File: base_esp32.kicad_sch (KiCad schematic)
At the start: 67 parts, among them J1 Input Source, J10 5V, J11 keypad, J12 keypad, J13 H_IO33, J14 H_IO15, J15 H_IO32, J16 H_IO02, J17 H_IO04, J18 H_IO33_OUT, J19 H_IO15_OUT, J2 Src Board, J20 H_IO32_OUT, J21 H_IO02_OUT, J22 H_IO04_OUT, J23 I2C, J24 I2C, J25 SPI, J26 SPI, J27 IO34, J28 IO35, J29 IO36, J3 5V, J30 IO39, J31 bypass, J4 5V, J5 5V, J6 5V, J7 5V, J8 5V, J9 5V, SW1 SW_DIP_KEYPAD, SW2 SW_DIP_INPUTS, SW3 Selector_Input, SW4 Selector_Input, SW5 INPUT_1, SW6 INPUT_2, SW7 RESET, SW8 BOOT, U1 LM7805_TO220, U2 ESP32-DevKitC, U3 AMS1117, U4 AMS1117

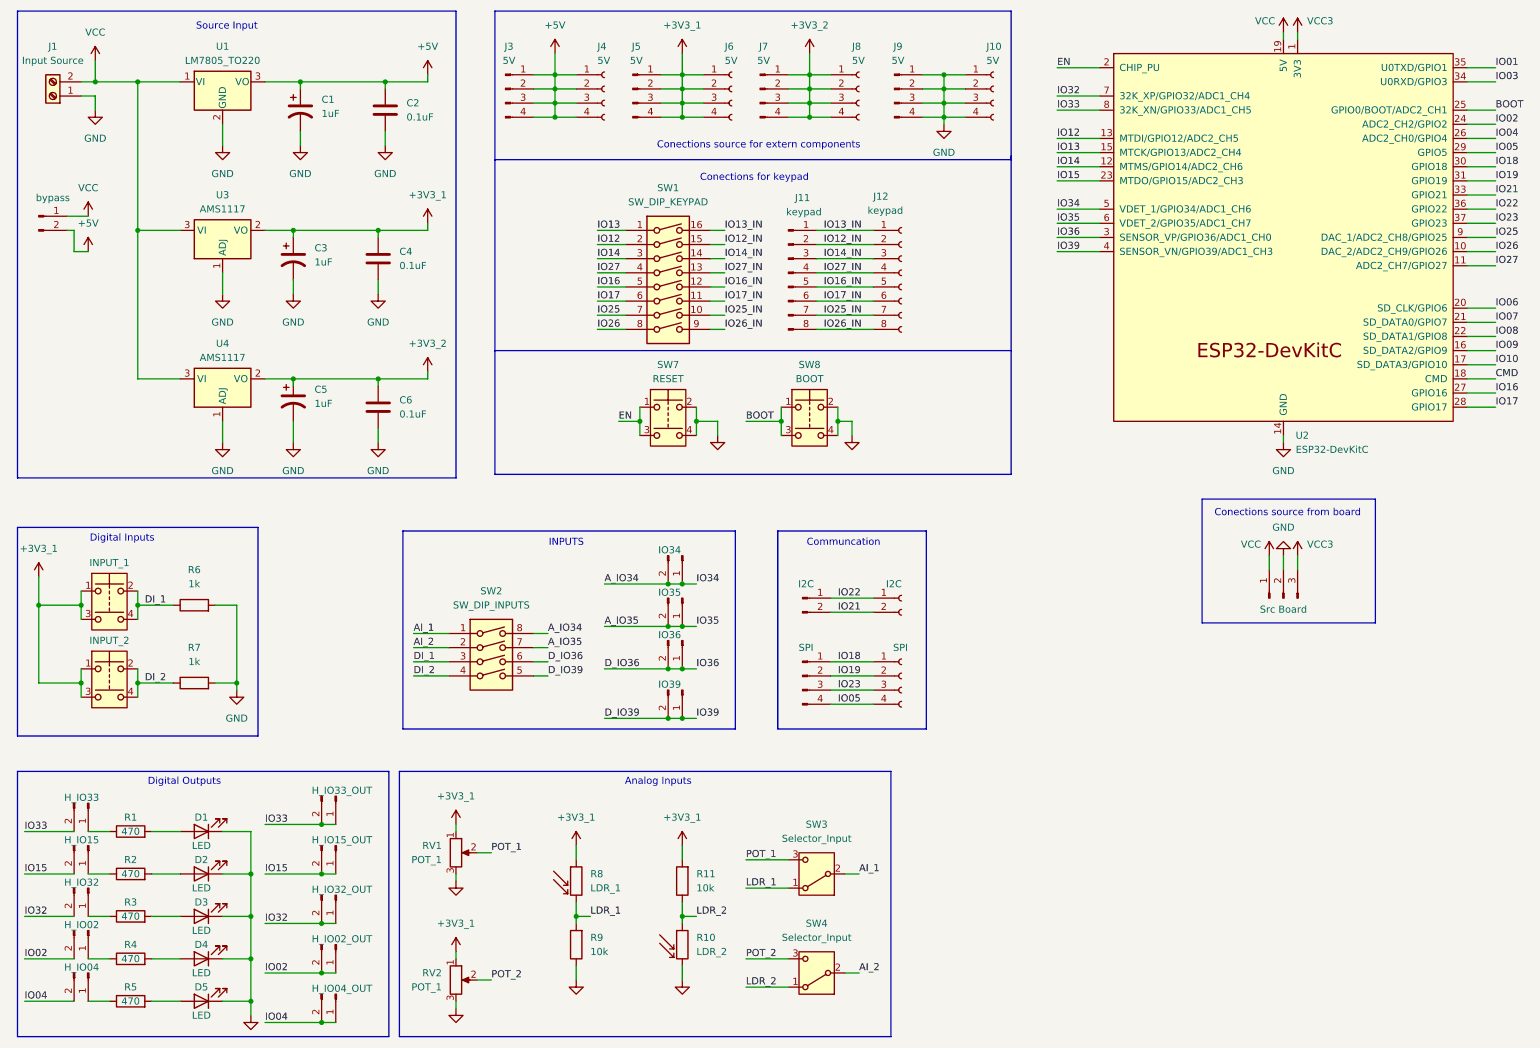
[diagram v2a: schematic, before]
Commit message: fix: vpp for board
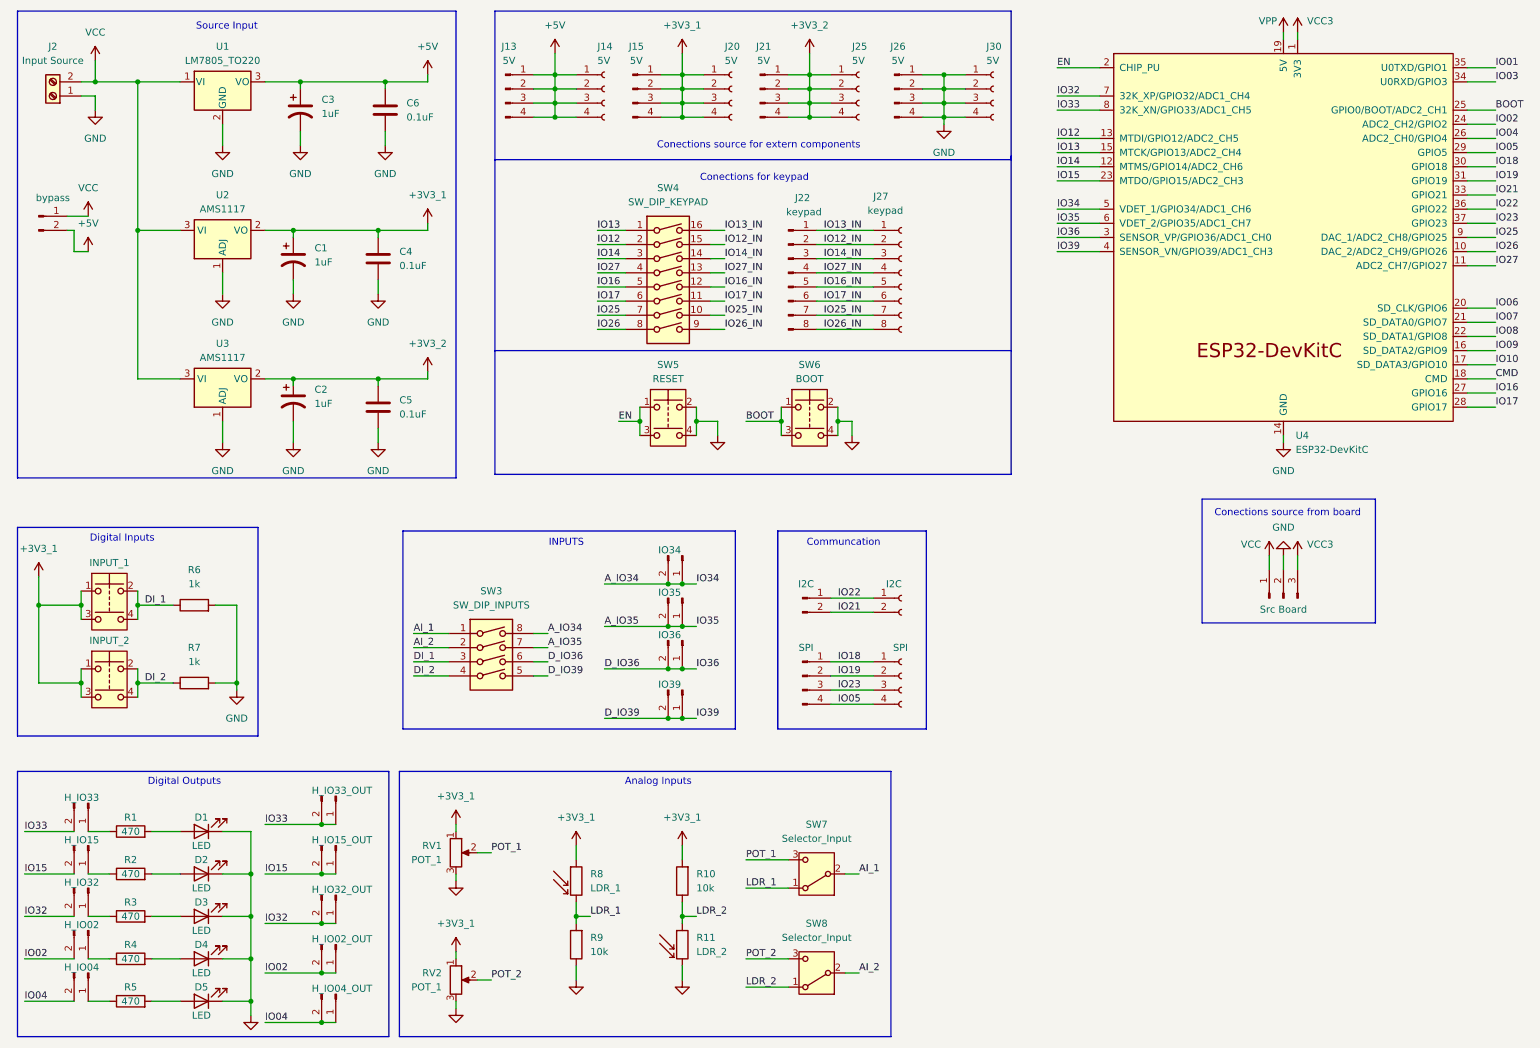
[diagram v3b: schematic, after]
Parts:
- renumbered C3 to C1, C5 to C2, C1 to C3, C6 to C5, C2 to C6, J31 to J1, J20 to J10, J21 to J11, J22 to J12, J3 to J13, J4 to J14, J5 to J15, J27 to J16, J28 to J17, J29 to J18, J30 to J19, J1 to J2, J6 to J20, J7 to J21, J11 to J22, J25 to J24, J8 to J25, J9 to J26, J12 to J27, J24 to J28, J26 to J29, J13 to J3, J10 to J30, J2 to J31, J14 to J4, J15 to J5, J16 to J6, J17 to J7, J18 to J8, J19 to J9, R11 to R10, R10 to R11, SW5 to SW1, SW6 to SW2, SW2 to SW3, SW1 to SW4, SW7 to SW5, SW8 to SW6, SW3 to SW7, SW4 to SW8, U3 to U2, U4 to U3, U2 to U4
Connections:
- net VCC: no longer U4.19 (5V)
- new net VPP: U4.19 (5V)

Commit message: fix: ERC
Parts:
- added J32: TX_RX, symbol Connector:Conn_01x02_Pin
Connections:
- net A_IO34 renamed IO34
- net A_IO35 renamed IO35
- net CMD: no longer names the net of U4.18 (CMD)
- net D_IO36 renamed IO36
- net D_IO39 renamed IO39
- net IO01 renamed TX
- net TX: now also J32.1 (Pin_1)
- net IO03 renamed RX
- net RX: now also J32.2 (Pin_2)
- net IO06: no longer names the net of U4.20 (SD_CLK/GPIO6)
- net IO07: no longer names the net of U4.21 (SD_DATA0/GPIO7)
- net IO08: no longer names the net of U4.22 (SD_DATA1/GPIO8)
- net IO09: no longer names the net of U4.16 (SD_DATA2/GPIO9)
- net IO10: no longer names the net of U4.17 (SD_DATA3/GPIO10)
- no-connect marks 0 -> 6
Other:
- note added: "Communication"
- note removed: "Communcation"

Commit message: add: footprints, not done yet
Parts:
- D1, D2, D3, D4, D5: footprint (none) -> LED_THT:LED_D3.0mm
- J1, J10, J11, J12, J16, J17, J18, J19, J23, J3, J32, J4, J5, J6, J7, J8, J9: footprint (none) -> Connector_PinHeader_1.27mm:PinHeader_1x02_P1.27mm_Vertical
- J13, J15, J21, J24, J26: footprint (none) -> Connector_PinHeader_1.27mm:PinHeader_1x04_P1.27mm_Vertical
- J14, J20, J25, J29, J30: footprint (none) -> Connector_PinSocket_1.27mm:PinSocket_1x04_P1.27mm_Vertical
- J2: footprint (none) -> TerminalBlock:TerminalBlock_Xinya_XY308-2.54-2P_1x02_P2.54mm_Horizontal
- J22: footprint (none) -> Connector_PinHeader_1.27mm:PinHeader_1x08_P1.27mm_Vertical
- J27: footprint (none) -> Connector_PinSocket_1.27mm:PinSocket_1x08_P1.27mm_Vertical
- J28: footprint (none) -> Connector_PinSocket_1.27mm:PinSocket_1x02_P1.27mm_Vertical
- J31: footprint (none) -> Connector_PinHeader_1.27mm:PinHeader_1x03_P1.27mm_Vertical
- RV1, RV2: footprint (none) -> Potentiometer_THT:Potentiometer_Alps_RK163_Single_Horizontal
- SW1, SW2, SW5, SW6: footprint (none) -> Button_Switch_THT:SW_PUSH_6mm
- SW3, SW4: footprint (none) -> Button_Switch_THT:SW_DIP_SPSTx04_Slide_9.78x12.34mm_W7.62mm_P2.54mm
- SW7, SW8: footprint (none) -> Button_Switch_THT:SW_Slide-03_Wuerth-WS-SLTV_10x2.5x6.4_P2.54mm
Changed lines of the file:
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@@
 			)
 		)
-		(property "Footprint" ""
+		(property "Footprint" "Connector_PinHeader_1.27mm:PinHeader_1x02_P1.27mm_Vertical"
 			(at 158.75 137.16 0)
 			(effects
@@
 			)
 		)
-		(property "Footprint" ""
+		(property "Footprint" "Connector_PinHeader_1.27mm:PinHeader_1x04_P1.27mm_Vertical"
 			(at 146.05 26.67 0)
 			(effects
@@
 			)
 		)
-		(property "Footprint" ""
+		(property "Footprint" "Connector_PinSocket_1.27mm:PinSocket_1x04_P1.27mm_Vertical"
 			(at 163.83 26.67 0)
 			(effects
@@
 			)
 		)
-		(property "Footprint" ""
+		(property "Footprint" "Connector_PinHeader_1.27mm:PinHeader_1x03_P1.27mm_Vertical"
 			(at 240.03 118.11 0)
 			(effects
@@
 			)
 		)
-		(property "Footprint" ""
+		(property "Footprint" "Connector_PinHeader_1.27mm:PinHeader_1x02_P1.27mm_Vertical"
 			(at 25.4 162.56 0)
 			(effects
@@
 			)
 		)
-		(property "Footprint" ""
+		(property "Footprint" "LED_THT:LED_D3.0mm"
 			(at 45.72 175.26 0)
 			(effects
@@
 			)
 		)
-		(property "Footprint" ""
+		(property "Footprint" "Connector_PinHeader_1.27mm:PinHeader_1x04_P1.27mm_Vertical"
 			(at 153.67 125.73 0)
 			(effects
@@
 			)
 		)
-		(property "Footprint" ""
+		(property "Footprint" "Connector_PinHeader_1.27mm:PinHeader_1x04_P1.27mm_Vertical"
 			(at 170.18 26.67 0)
 			(effects
@@
 			)
 		)
-		(property "Footprint" ""
+		(property "Footprint" "Button_Switch_THT:SW_DIP_SPSTx04_Slide_9.78x12.34mm_W7.62mm_P2.54mm"
 			(at 129.54 62.23 0)
 			(effects
@@
 			)
 		)
-		(property "Footprint" ""
+		(property "Footprint" "Connector_PinSocket_1.27mm:PinSocket_1x04_P1.27mm_Vertical"
 			(at 187.96 26.67 0)
 			(effects
@@
 			)
 		)
-		(property "Footprint" ""
+		(property "Footprint" "Connector_PinHeader_1.27mm:PinHeader_1x02_P1.27mm_Vertical"
 			(at 25.4 170.18 0)
 			(effects
@@
 			)
 		)
-		(property "Footprint" ""
+		(property "Footprint" "Connector_PinHeader_1.27mm:PinHeader_1x02_P1.27mm_Vertical"
 			(at 132.08 118.11 0)
 			(effects
@@
 			)
 		)
-		(property "Footprint" ""
+		(property "Footprint" "Connector_PinHeader_1.27mm:PinHeader_1x02_P1.27mm_Vertical"
 			(at 69.85 189.23 0)
 			(effects
@@
 			)
 		)
-		(property "Footprint" ""
+		(property "Footprint" "LED_THT:LED_D3.0mm"
 			(at 45.72 167.64 0)
 			(effects
@@
 			)
 		)
-		(property "Footprint" ""
+		(property "Footprint" "Connector_PinHeader_1.27mm:PinHeader_1x02_P1.27mm_Vertical"
 			(at 69.85 180.34 0)
 			(effects
@@
 			)
 		)
-		(property "Footprint" ""
+		(property "Footprint" "Button_Switch_THT:SW_DIP_SPSTx04_Slide_9.78x12.34mm_W7.62mm_P2.54mm"
 			(at 97.79 129.54 0)
 			(effects
@@
 			)
 		)
-		(property "Footprint" ""
+		(property "Footprint" "LED_THT:LED_D3.0mm"
 			(at 45.72 160.02 0)
 			(effects
@@
 			)
 		)
-		(property "Footprint" ""
+		(property "Footprint" "Connector_PinSocket_1.27mm:PinSocket_1x04_P1.27mm_Vertical"
 			(at 140.97 26.67 0)
 			(effects
@@
 			)
 		)
-		(property "Footprint" ""
+		(property "Footprint" "Connector_PinHeader_1.27mm:PinHeader_1x02_P1.27mm_Vertical"
 			(at 69.85 153.67 0)
 			(effects
@@
 			)
 		)
-		(property "Footprint" ""
+		(property "Footprint" "Button_Switch_THT:SW_PUSH_6mm"
 			(at 154.94 78.74 0)
 			(effects
@@
 			)
 		)
-		(property "Footprint" ""
+		(property "Footprint" "Connector_PinHeader_1.27mm:PinHeader_1x04_P1.27mm_Vertical"
 			(at 100.33 26.67 0)
 			(effects
@@
 			)
 		)
-		(property "Footprint" ""
+		(property "Footprint" "Connector_PinHeader_1.27mm:PinHeader_1x04_P1.27mm_Vertical"
 			(at 123.19 26.67 0)
 			(effects
@@
 			)
 		)
-		(property "Footprint" ""
+		(property "Footprint" "Connector_PinHeader_1.27mm:PinHeader_1x02_P1.27mm_Vertical"
 			(at 132.08 134.62 0)
 			(effects
@@
 			)
 		)
-		(property "Footprint" ""
+		(property "Footprint" "Button_Switch_THT:SW_PUSH_6mm"
 			(at 29.21 111.76 0)
 			(effects
@@
 			)
 		)
-		(property "Footprint" ""
+		(property "Footprint" "Connector_PinHeader_1.27mm:PinHeader_1x02_P1.27mm_Vertical"
 			(at 153.67 114.3 0)
 			(effects
@@
 			)
 		)
-		(property "Footprint" ""
+		(property "Footprint" "Potentiometer_THT:Potentiometer_Alps_RK163_Single_Horizontal"
 			(at 91.44 163.83 0)
 			(effects
@@
 			)
 		)
-		(property "Footprint" ""
+		(property "Footprint" "Connector_PinSocket_1.27mm:PinSocket_1x08_P1.27mm_Vertical"
 			(at 171.45 59.69 0)
 			(effects
@@
 			)
 		)
-		(property "Footprint" ""
+		(property "Footprint" "LED_THT:LED_D3.0mm"
 			(at 45.72 190.5 0)
 			(effects
@@
 			)
 		)
-		(property "Footprint" ""
+		(property "Footprint" "Connector_PinHeader_1.27mm:PinHeader_1x02_P1.27mm_Vertical"
 			(at 25.4 154.94 0)
 			(effects
@@
 			)
 		)
-		(property "Footprint" ""
+		(property "Footprint" "Connector_PinSocket_1.27mm:PinSocket_1x04_P1.27mm_Vertical"
 			(at 171.45 125.73 0)
 			(effects
@@
 			)
 		)
-		(property "Footprint" ""
+		(property "Footprint" "TerminalBlock:TerminalBlock_Xinya_XY308-2.54-2P_1x02_P2.54mm_Horizontal"
 			(at 19.05 27.94 0)
 			(effects
@@
 			)
 		)
-		(property "Footprint" ""
+		(property "Footprint" "Connector_PinHeader_1.27mm:PinHeader_1x02_P1.27mm_Vertical"
 			(at 25.4 185.42 0)
 			(effects
@@
 			)
 		)
-		(property "Footprint" ""
+		(property "Footprint" "Connector_PinHeader_1.27mm:PinHeader_1x08_P1.27mm_Vertical"
 			(at 151.13 59.69 0)
 			(effects
@@
 			)
 		)
-		(property "Footprint" ""
+		(property "Footprint" "Connector_PinHeader_1.27mm:PinHeader_1x02_P1.27mm_Vertical"
 			(at 69.85 171.45 0)
 			(effects
@@
 			)
 		)
-		(property "Footprint" ""
+		(property "Footprint" "Button_Switch_THT:SW_PUSH_6mm"
 			(at 129.54 78.74 0)
 			(effects
@@
 			)
 		)
-		(property "Footprint" ""
+		(property "Footprint" "Potentiometer_THT:Potentiometer_Alps_RK163_Single_Horizontal"
 			(at 91.44 186.69 0)
 			(effects
@@
 			)
 		)
-		(property "Footprint" ""
+		(property "Footprint" "LED_THT:LED_D3.0mm"
 			(at 45.72 182.88 0)
 			(effects
@@
 			)
 		)
-		(property "Footprint" ""
+		(property "Footprint" "Connector_PinHeader_1.27mm:PinHeader_1x02_P1.27mm_Vertical"
 			(at 132.08 110.49 0)
 			(effects
@@
 			)
 		)
-		(property "Footprint" ""
+		(property "Footprint" "Connector_PinHeader_1.27mm:PinHeader_1x02_P1.27mm_Vertical"
 			(at 16.51 49.53 0)
 			(effects
@@
 			)
 		)
-		(property "Footprint" ""
+		(property "Footprint" "Button_Switch_THT:SW_Slide-03_Wuerth-WS-SLTV_10x2.5x6.4_P2.54mm"
 			(at 156.21 167.64 0)
 			(effects
@@
 			)
 		)
-		(property "Footprint" ""
+		(property "Footprint" "Connector_PinSocket_1.27mm:PinSocket_1x02_P1.27mm_Vertical"
 			(at 171.45 114.3 0)
 			(effects
@@
 			)
 		)
-		(property "Footprint" ""
+		(property "Footprint" "Connector_PinHeader_1.27mm:PinHeader_1x02_P1.27mm_Vertical"
 			(at 25.4 177.8 0)
 			(effects
@@
 			)
 		)
-		(property "Footprint" ""
+		(property "Footprint" "Connector_PinHeader_1.27mm:PinHeader_1x02_P1.27mm_Vertical"
 			(at 132.08 125.73 0)
 			(effects
@@
 			)
 		)
-		(property "Footprint" ""
+		(property "Footprint" "Button_Switch_THT:SW_Slide-03_Wuerth-WS-SLTV_10x2.5x6.4_P2.54mm"
 			(at 156.21 185.42 0)
 			(effects
@@
 			)
 		)
-		(property "Footprint" ""
+		(property "Footprint" "Connector_PinSocket_1.27mm:PinSocket_1x04_P1.27mm_Vertical"
 			(at 118.11 26.67 0)
 			(effects
@@
 			)
 		)
-		(property "Footprint" ""
+		(property "Footprint" "Button_Switch_THT:SW_PUSH_6mm"
 			(at 29.21 125.73 0)
 			(effects
@@
 			)
 		)
-		(property "Footprint" ""
+		(property "Footprint" "Connector_PinHeader_1.27mm:PinHeader_1x02_P1.27mm_Vertical"
 			(at 69.85 162.56 0)
 			(effects

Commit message: fix: schematic & footprint done
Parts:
- removed J1: bypass, Connector_PinHeader_1.27mm:PinHeader_1x02_P1.27mm_Vertical, symbol Connector:Conn_01x02_Pin
- removed SW1: INPUT_1, Button_Switch_THT:SW_PUSH_6mm, symbol Switch:SW_Push_Dual
- removed SW2: INPUT_2, Button_Switch_THT:SW_PUSH_6mm, symbol Switch:SW_Push_Dual
- removed SW5: RESET, Button_Switch_THT:SW_PUSH_6mm, symbol Switch:SW_Push_Dual
- removed SW6: BOOT, Button_Switch_THT:SW_PUSH_6mm, symbol Switch:SW_Push_Dual
- added D6, D7: LED, LED_THT:LED_D3.0mm, symbol Device:LED
- added J2: BYPASS_SRC_5V, Connector_PinHeader_1.27mm:PinHeader_1x03_P1.27mm_Vertical, symbol Connector:Conn_01x03_Pin
- added J3: BYPASS_SRC_3V3, Connector_PinHeader_1.00mm:PinHeader_1x04_P1.00mm_Vertical, symbol Connector:Conn_01x04_Pin
- added R12, R13: 1k, Resistor_THT:R_Axial_DIN0207_L6.3mm_D2.5mm_P10.16mm_Horizontal, symbol Device:R
- added SW1: INPUT_D1, Button_Switch_THT:SW_PUSH_6mm, symbol Switch:SW_Push
- added SW2: INPUT_D2, Button_Switch_THT:SW_PUSH_6mm, symbol Switch:SW_Push
- added SW4: ENABLE, Button_Switch_THT:SW_PUSH_6mm, symbol Switch:SW_Push
- added SW8: BOOT, Button_Switch_THT:SW_PUSH_6mm, symbol Switch:SW_Push
- C1, C2, C3: footprint (none) -> Capacitor_THT:CP_Radial_D5.0mm_P2.50mm
- C4, C5, C6: footprint (none) -> Capacitor_THT:C_Disc_D5.0mm_W2.5mm_P5.00mm
- J16: renamed from J15; value 5V -> H_3V3_1
- J17: renamed from J16; value IO34 -> H_IO34
- J18: renamed from J17; value IO35 -> H_IO35
- J19: renamed from J18; value IO36 -> H_IO36
- J20: renamed from J19; value IO39 -> H_IO39
- J21: renamed from J20; value 5V -> S_3V3_1
- J22: renamed from J21; value 5V -> H_3V3_2
- J23: renamed from J22; value keypad -> H_KEYPAD
- J24: renamed from J23; value I2C -> H_I2C
- J25: renamed from J24; value SPI -> H_SPI
- J27: renamed from J25; value 5V -> S_3V3_2
- J28: renamed from J26; value 5V -> H_GND
- J29: renamed from J27; value keypad -> S_KEYPAD
- J30: renamed from J28; value I2C -> S_I2C
- J31: renamed from J29; value SPI -> S_SPI
- J32: renamed from J30; value 5V -> S_GND
- R1, R10, R2, R3, R4, R5, R6, R7, R9: footprint (none) -> Resistor_THT:R_Axial_DIN0207_L6.3mm_D2.5mm_P10.16mm_Horizontal
- renumbered J2 to J1, J9 to J10, J10 to J11, J11 to J12, J12 to J13, J13 to J14, J14 to J15, J32 to J26, J31 to J33, J3 to J4, J4 to J5, J5 to J6, J6 to J7, J7 to J8, J8 to J9, SW4 to SW5, SW7 to SW6, SW8 to SW7
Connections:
- net +3V3_1: now also J3.2 (Pin_2), SW1.1, SW2.1
- net +3V3_2: now also J3.4 (Pin_4)
- net +5V: now also J2.2 (Pin_2)
- net BOOT: now also SW8.1
- net DI_1: now also SW1.2
- net DI_2: now also SW2.2
- net EN: now also SW4.1
- net GND: now also D6.1 (K), D7.1 (K), SW4.2, SW8.2
- net VCC: now also J2.1 (Pin_1), R12.1, R13.1
- net VCC3: now also J3.1 (Pin_1), J3.3 (Pin_3)
- net VPP: now also J2.3 (Pin_3)
- new net: D6.2 (A), R12.2
- new net: D7.2 (A), R13.2
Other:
- note added: "Power Board"
- note added: "Power ext"
- moved on the sheet: R6, R7

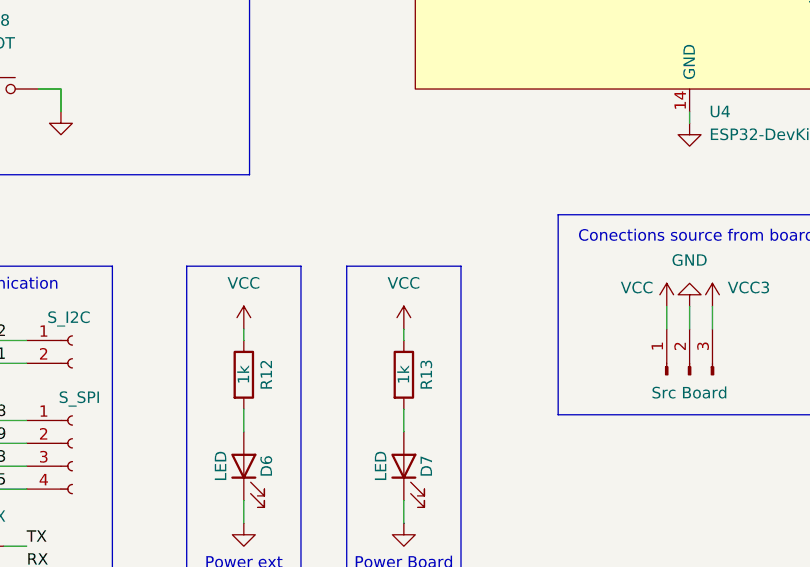
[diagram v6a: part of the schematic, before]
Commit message: add: led to power board
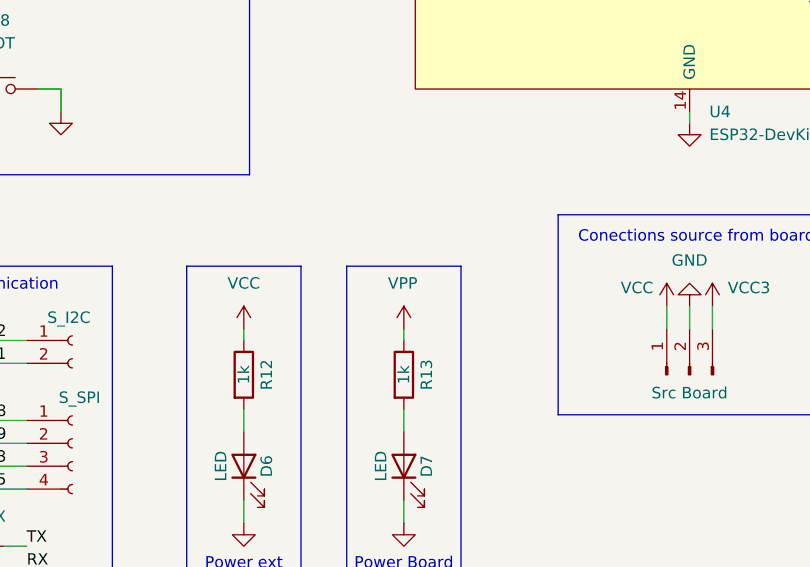
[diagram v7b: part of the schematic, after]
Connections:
- net VCC: no longer R13.1
- net VPP: now also R13.1
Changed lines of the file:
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@@
 		(on_board yes)
 		(dnp no)
-		(fields_autoplaced yes)
 		(property "Reference" "#PWR040"
 			(at 208.28 116.84 0)
@@
 			)
 		)
-		(property "Value" "VCC"
-			(at 208.28 107.95 0)
+		(property "Value" "VPP"
+			(at 206.502 107.95 0)
 			(effects
 				(font
 					(size 1.27 1.27)
 				)
+				(justify left)
 			)
 		)
